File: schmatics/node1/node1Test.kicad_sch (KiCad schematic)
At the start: 5 parts, among them J1 MAX6675, J2 WCS1800, J3 MAX6675, J4 MAX6675

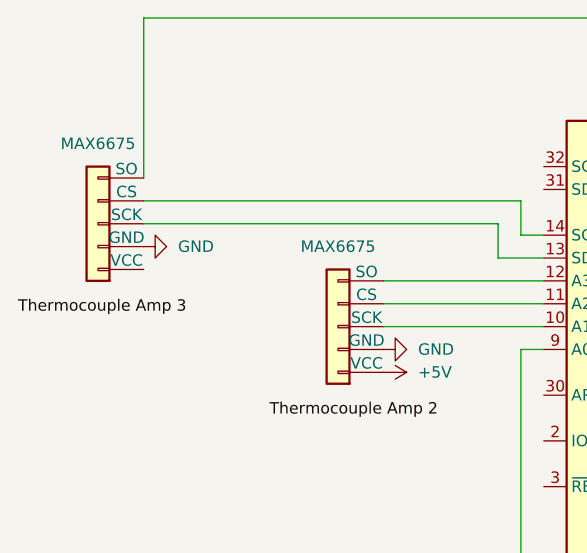
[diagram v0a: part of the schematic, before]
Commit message: Added node1 thermocouplesupport
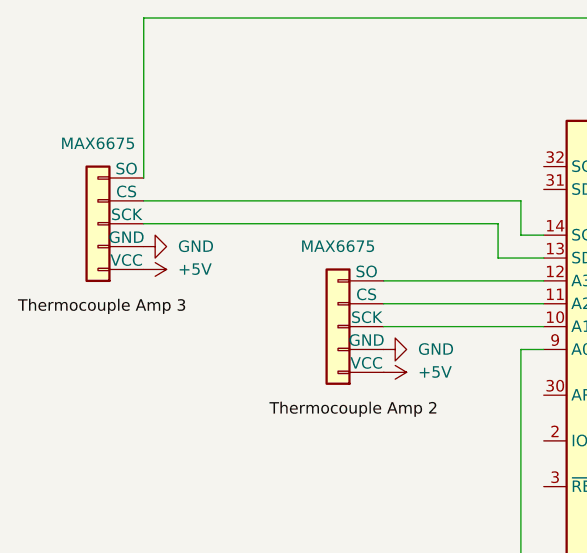
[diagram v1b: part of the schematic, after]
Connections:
- net +5V: now also J4.1 (VCC)
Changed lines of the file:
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@@
+	)
+	(symbol
+		(lib_id "power:+5V")
+		(at 48.26 45.72 270)
+		(unit 1)
+		(body_style 1)
+		(exclude_from_sim no)
+		(in_bom yes)
+		(on_board yes)
+		(in_pos_files yes)
+		(dnp no)
+		(fields_autoplaced yes)
+		(property "Reference" "#PWR07"
+			(at 44.45 45.72 0)
+			(hide yes)
+			(show_name no)
+			(do_not_autoplace no)
+			(effects
+				(font
+					(size 1.27 1.27)
+				)
+			)
+		)
+		(property "Value" "+5V"
+			(at 52.07 45.7199 90)
+			(show_name no)
+			(do_not_autoplace no)
+			(effects
+				(font
+					(size 1.27 1.27)
+				)
+				(justify left)
+			)
+		)
+		(property "Footprint" ""
+			(at 48.26 45.72 0)
+			(hide yes)
+			(show_name no)
+			(do_not_autoplace no)
+			(effects
+				(font
+					(size 1.27 1.27)
+				)
+			)
+		)
+		(property "Datasheet" ""
+			(at 48.26 45.72 0)
+			(hide yes)
+			(show_name no)
+			(do_not_autoplace no)
+			(effects
+				(font
+					(size 1.27 1.27)
+				)
+			)
+		)
+		(property "Description" "Power symbol creates a global label with name \"+5V\""
+			(at 48.26 45.72 0)
+			(hide yes)
+			(show_name no)
+			(do_not_autoplace no)
+			(effects
+				(font
+					(size 1.27 1.27)
+				)
+			)
+		)
+		(pin "1"
+		)
+		(instances
+			(project "node1Test"
+				(path "/6e48e298-eaa0-44a2-9bd7-feda466659e2"
+					(reference "#PWR07")
+					(unit 1)
+				)
+			)
+		)
 	)
 	(symbol
